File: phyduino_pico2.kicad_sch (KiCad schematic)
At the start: 16 parts, among them J2 PPPC081LFBN-RC, J3 PPPC101LFBN-RC, J4 PPPC061LFBN-RC, J5 PPPC081LFBN-RC, J6 GT-USB-7047A, J7 HC-FPC-0.5-22P-CSH20, J8 54-00127, J9 SM04B-SRSS-TB, U9 TPUSBLC6-2P6

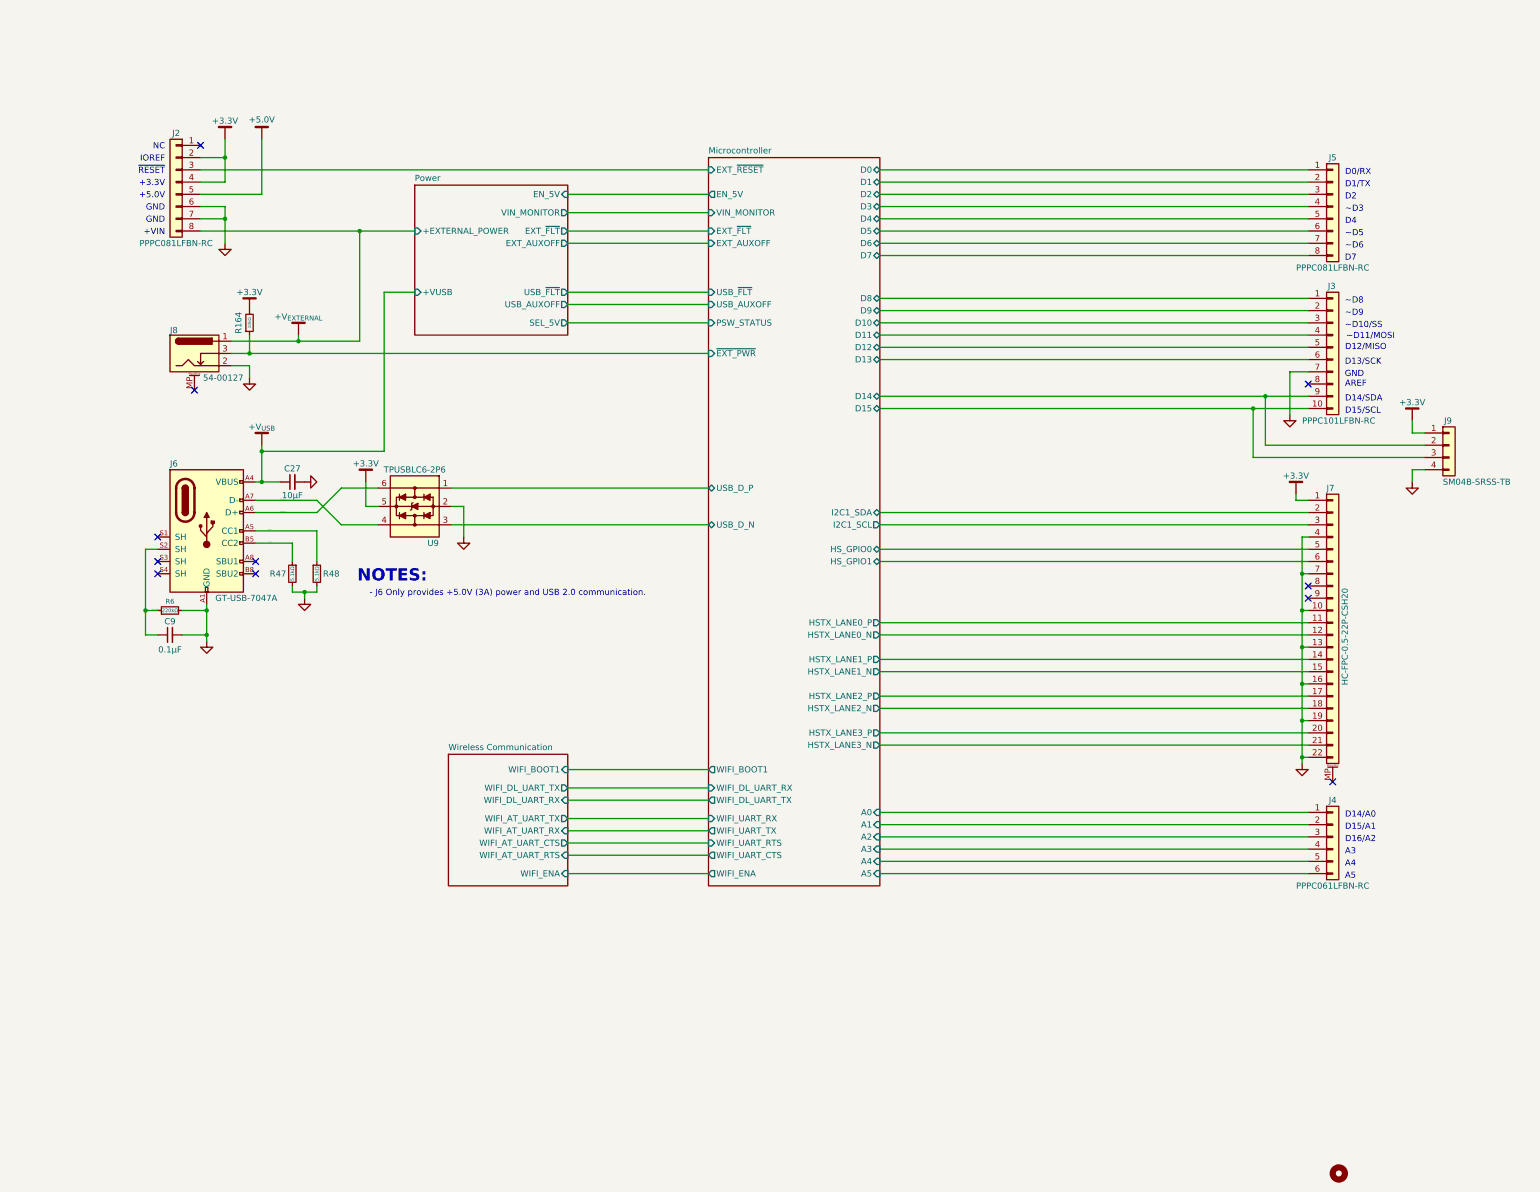
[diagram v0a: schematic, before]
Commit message: Resized schematic sheet to A from B. Add micropython logo to back silkscreen. Regenerated gerber files
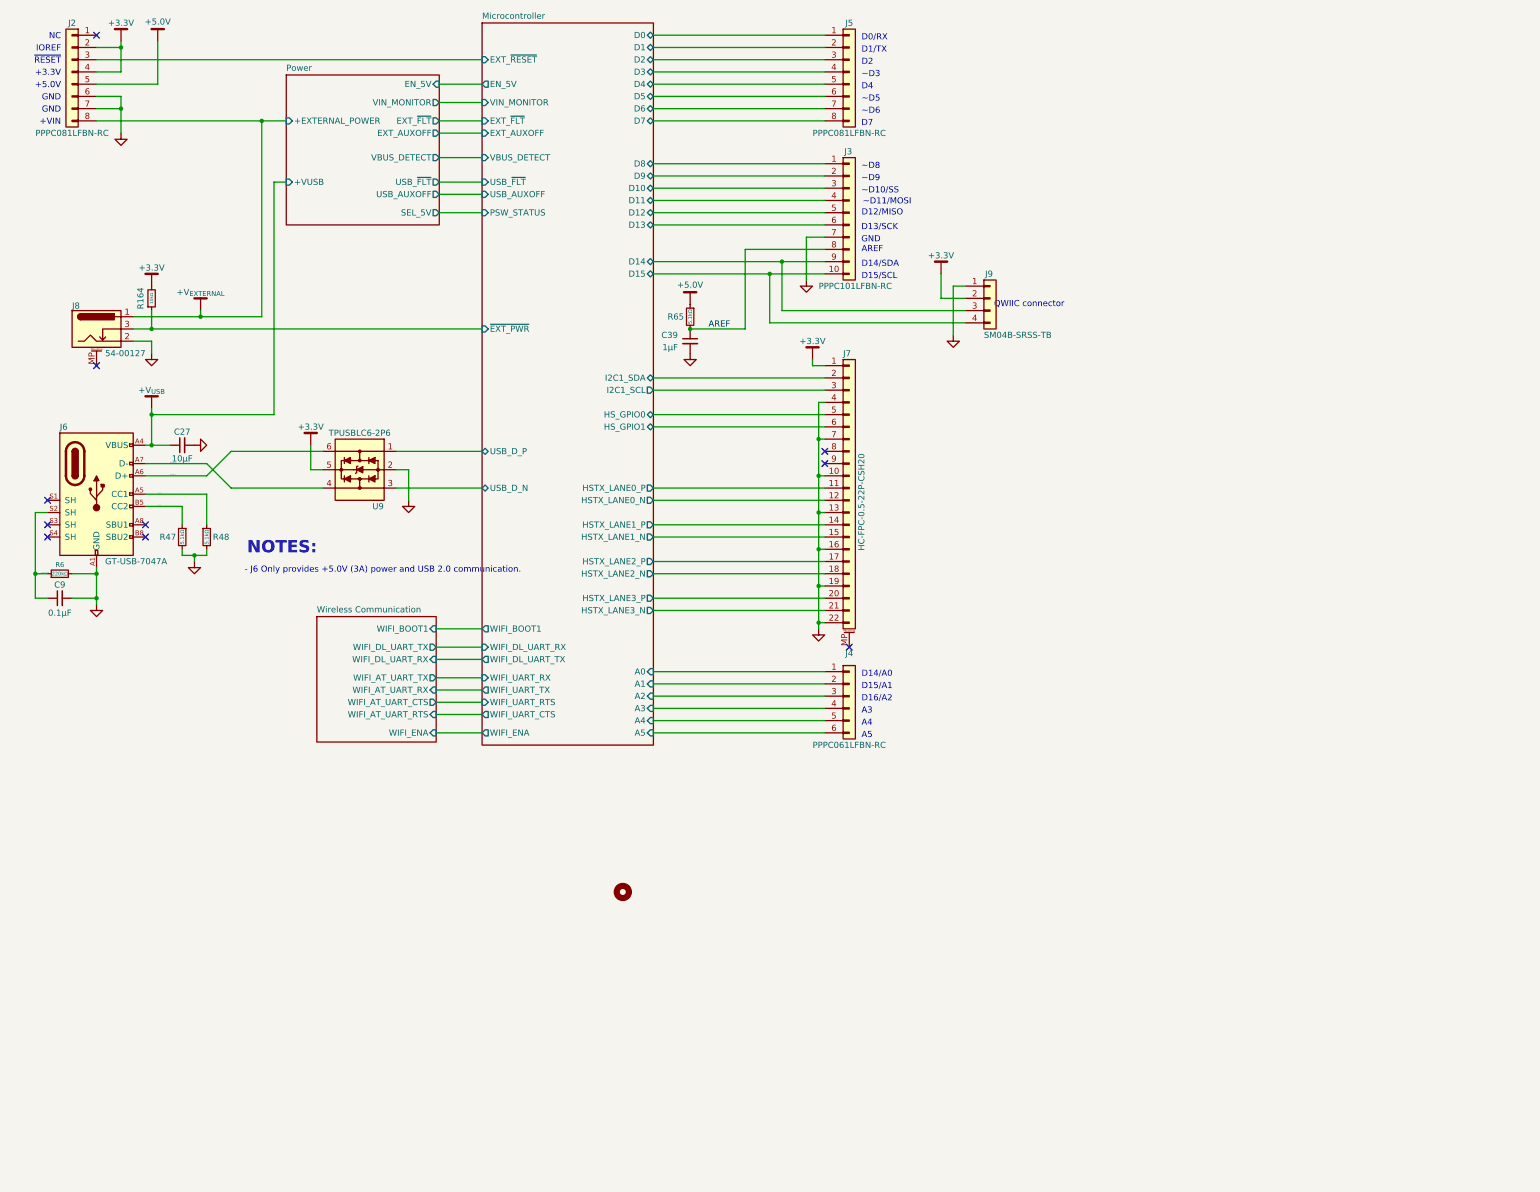
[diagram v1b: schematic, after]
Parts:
- added C39: 1µF, Capacitor_SMD:C_0402_1005Metric, symbol Component - Device [KL]:C_Small
- added R65: 5.1kΩ, Resistor_SMD:R_0402_1005Metric, symbol phyduino_pico:R_Small
- H2: footprint MountingHole [KL]:MountingHole_3.2mm_M3 -> MountingHole:MountingHole_3.2mm_M3
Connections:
- net +3.3V: now also J9.2 (Pin_2); no longer J9.1 (Pin_1)
- net +5.0V: now also R65.1
- net GND: now also J9.1 (Pin_1), C39.2; no longer J9.4 (Pin_4)
- net Microcontroller/D14: now also J9.3 (Pin_3); no longer J9.2 (Pin_2)
- net Microcontroller/D15: now also J9.4 (Pin_4); no longer J9.3 (Pin_3)
- net AREF: now reaches J3.8 (Pin_8)
- net AREF: now also C39.1, R65.2
- no-connect marks 11 -> 10
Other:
- sheet Microcontroller ports: added VBUS_DETECT; removed none
- sheet Power ports: added VBUS_DETECT; removed none
- note added: "QWIIC connector"
- moved on the sheet: C27, C9, J2, J3, J4, J5, J6, J7, J8, J9, R164, R47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
